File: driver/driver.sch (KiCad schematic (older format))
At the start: 103 parts, among them J1 OUT_A, J10 FAN, J2 OUT_B, J4 RJ45_LED_Shielded, J5 RJ45_LED_Shielded, J6 1602 I2C LCD, J7 IN_VCC, J8 IN_GND, J9 SWD, Q1 TPHR6503PL, Q2 TPHR6503PL, Q3 TPHR6503PL, Q4 TPHR6503PL, U1 MT3608, U10 PC817, U11 AMS1117-5.0, U12 PC817, U13 MAX485E, U2 74HC595, U3 AMS1117-3.3, U4 TC4427, U5 TC4427, U6 STM32F030F4Px, U7 INA226, U8 MCP9804_MSOP, U9 PC817, Y1 8MHz

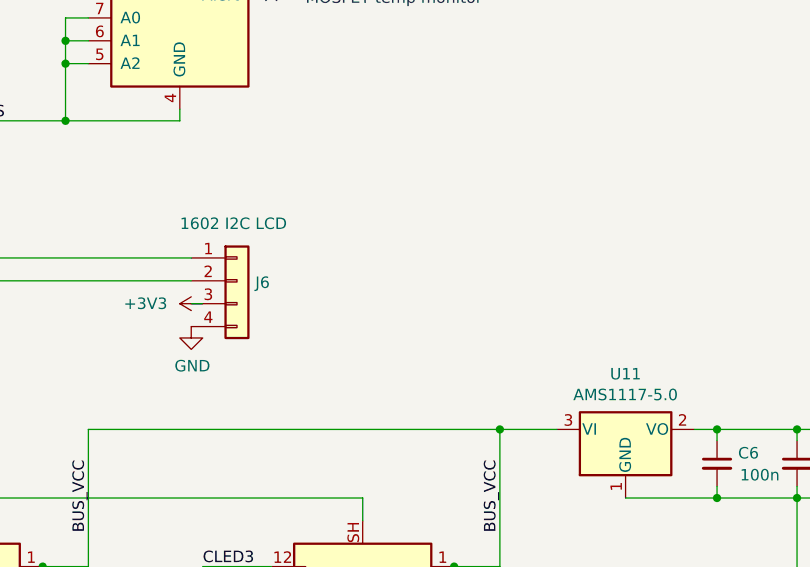
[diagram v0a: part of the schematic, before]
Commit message: driver/fw: Add tiny printf
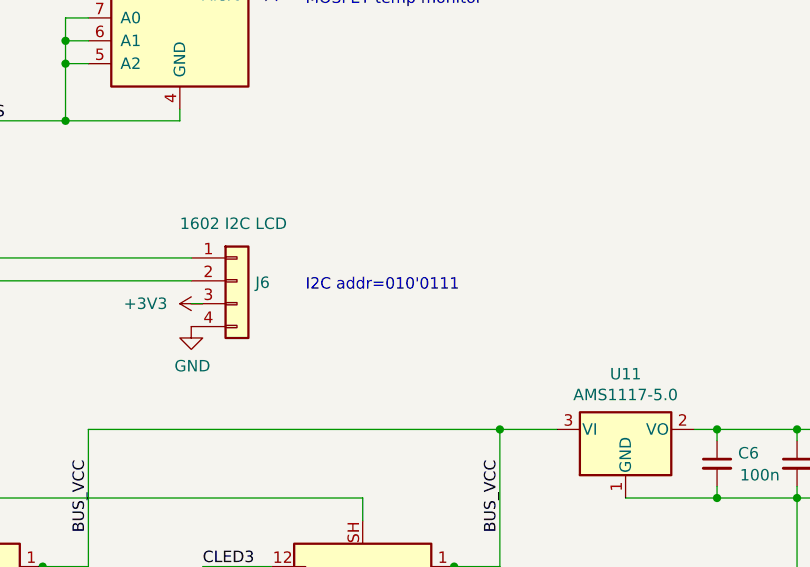
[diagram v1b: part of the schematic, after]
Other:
- note added: "I2C addr=010'0111"
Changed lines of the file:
@@
 TODO:\n* RS485 drv fp is wide, should be narrow SOIC-8\n* Heatsink holes are plated-through, shouln't be\n* Add thermal reliefs in upper logic ground plane\n* GND/VCC input labels are swapped\n* White label field for MAC\n* Remove optoisolators\n* Add series resistor to RS485 GND\n* Add decoupling cap next to mosfet temp sensor\n* Add INA226 filter network (see datasheet p.14)
 NoConn ~ 14600 2800
+Text Notes 14100 9650 0    50   ~ 0
+I2C addr=010'0111
 $EndSCHEMATC
